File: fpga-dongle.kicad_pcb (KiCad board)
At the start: 2 copper layers, 85.8 x 137 mm, 119 parts, among them P1 USB_PWR, P2 PGM, P3 right, P4 left, P5 CONN_01X40, P6 CONN_01X40, P7 DBG_SWD, P8 USB_PWR, Q1 BC857, SW1 T1107A(6x3,8x2,5MM)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

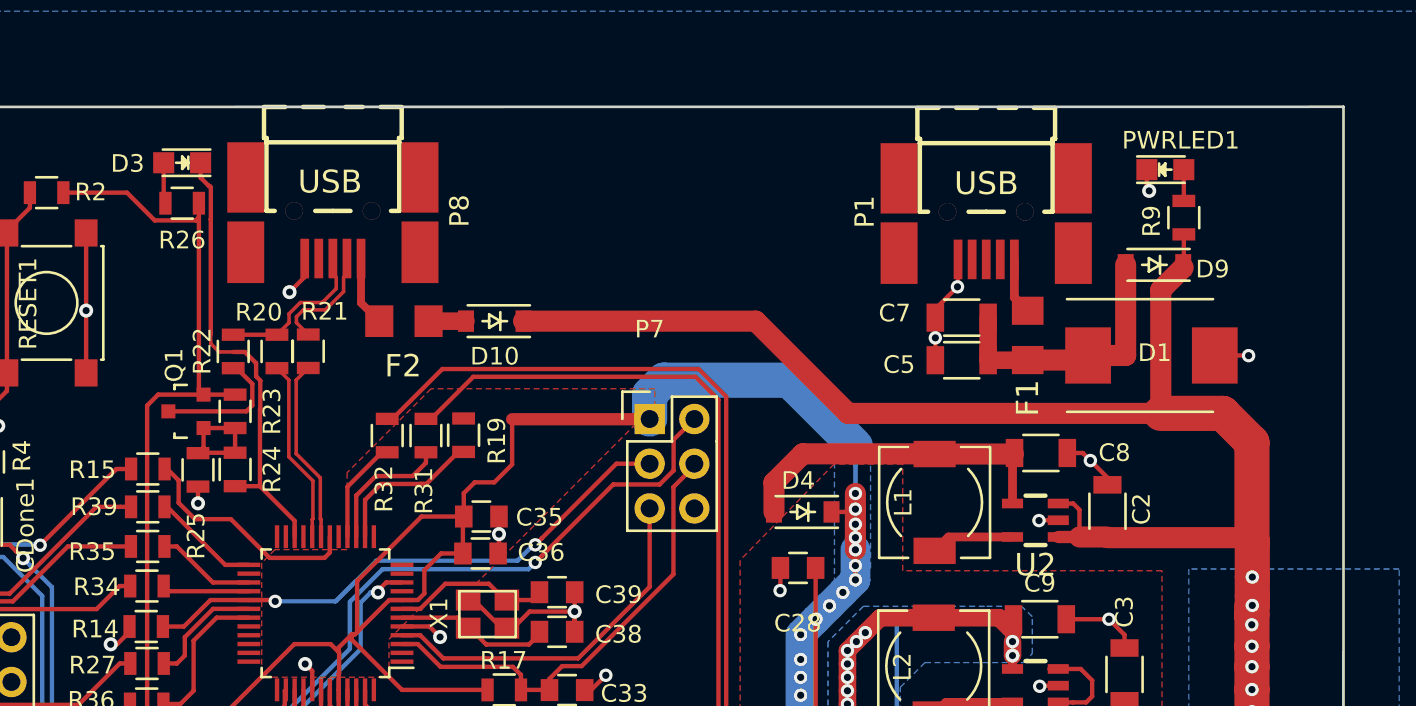
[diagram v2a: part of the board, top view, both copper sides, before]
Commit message: Change USB power-only connector by screw connector
Signed-off-by: Martin Ribelotta <martinribelotta@gmail.com>
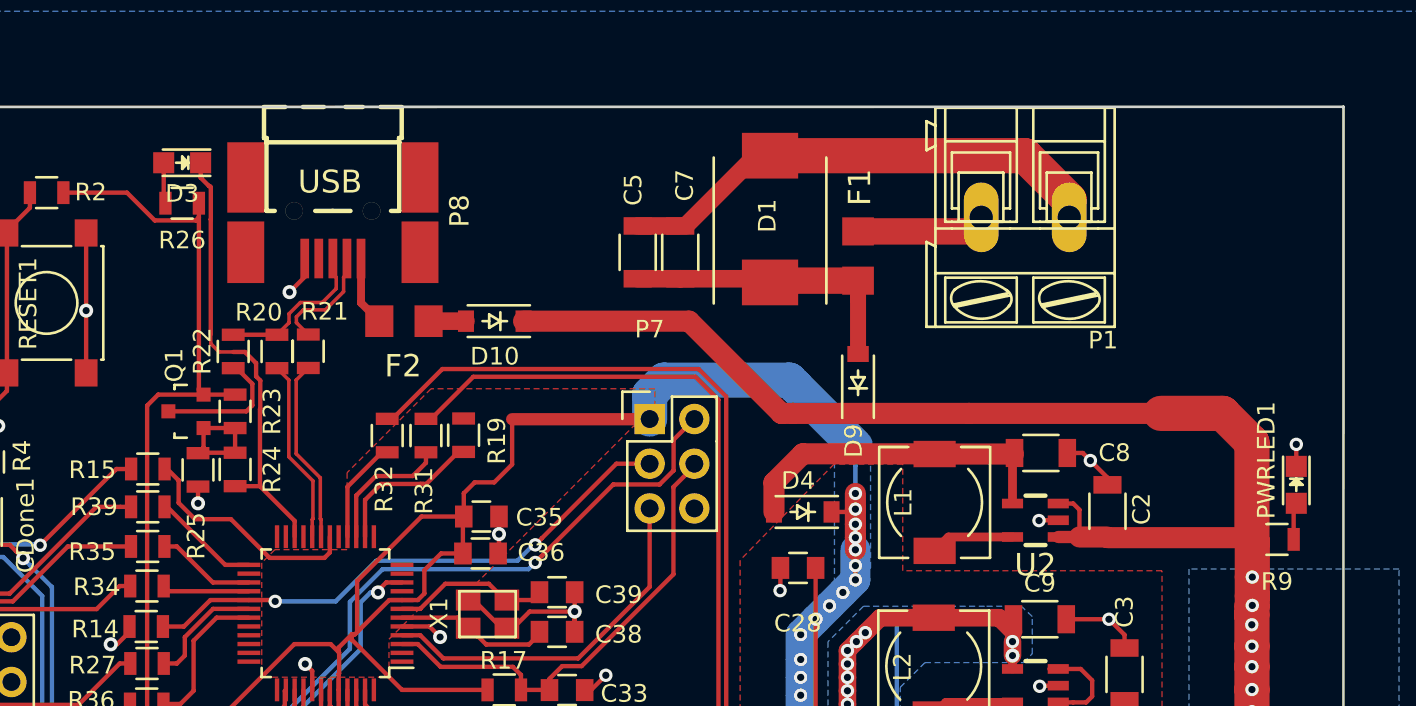
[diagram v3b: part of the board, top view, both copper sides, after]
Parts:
- D3: footprint LEDs:LED-0805 -> LEDs:LED_0805
- P1: value USB_PWR -> CONN_01X02; footprint OLIMEX_Connectors-FP:USB_Mini-B-NOSILK -> Connect:AK300-2
- moved D1 23.0 mm to (68.5, 24.0), turned to 90 degrees
- moved C5 19.4 mm to (61.0, 25.9), turned to 270 degrees
- moved PWRLED1 19.4 mm to (98.4, 39.1), turned to 270 degrees
- moved R9 19.0 mm to (97.3, 42.2), turned to 0 degrees
- moved D9 18.1 mm to (73.5, 33.3), turned to 90 degrees
- moved C7 16.4 mm to (63.4, 25.9), turned to 270 degrees
- moved F1 10.6 mm to (73.5, 26.1)
- moved P1 4.73 mm to (85.5, 23.9), turned to 180 degrees
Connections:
- P1 pad 1: Net-(F1-Pad1) -> GND
- P1 pad 2: (no net) -> Net-(F1-Pad1)
- P2 pad 7: (no net) -> Net-(P2-Pad7)
- P3 pad 10: (no net) -> Net-(P3-Pad10)
- P3 pad 22: (no net) -> /LCD4
- P3 pad 24: (no net) -> /LCD_RS
- P3 pad 26: (no net) -> /LCD3
- P3 pad 28: (no net) -> /LCD2
- P3 pad 30: (no net) -> /LCD1
- P3 pad 31: (no net) -> /GPIO2
- P3 pad 32: (no net) -> /GPIO1
- P3 pad 33: (no net) -> /GPIO4
- P3 pad 34: (no net) -> /GPIO3
- P3 pad 35: (no net) -> /GPIO6
- P3 pad 36: (no net) -> /GPIO5
- P3 pad 38: (no net) -> /GPIO7
- P3 pad 40: (no net) -> /GPIO8
- P3 pad 8: (no net) -> Net-(P3-Pad8)
- P3 pad 9: (no net) -> Net-(P3-Pad9)
- P4 pad 11: (no net) -> Net-(P4-Pad11)
- P4 pad 13: (no net) -> Net-(P4-Pad13)
- P4 pad 15: (no net) -> Net-(P4-Pad15)
- P4 pad 17: (no net) -> Net-(P4-Pad17)
- P4 pad 27: (no net) -> /CAN_RD
- P4 pad 29: (no net) -> /CAN_TD
- P4 pad 3: (no net) -> Net-(P4-Pad3)
- P4 pad 31: (no net) -> /T_COL1
- P4 pad 33: (no net) -> /T_FIL0
- P4 pad 34: (no net) -> /T_COL2
- P4 pad 35: (no net) -> /T_FIL3
- P4 pad 36: (no net) -> /T_FIL1
- P4 pad 37: (no net) -> /T_FIL2
- P4 pad 39: (no net) -> /T_COL0
- P4 pad 5: (no net) -> Net-(P4-Pad5)
- P4 pad 6: (no net) -> Net-(P4-Pad6)
- P4 pad 7: (no net) -> Net-(P4-Pad7)
- P4 pad 9: (no net) -> Net-(P4-Pad9)
- P5 pad 35: (no net) -> Net-(P5-Pad35)
- P5 pad 36: (no net) -> Net-(P5-Pad36)
- P5 pad 5: (no net) -> Net-(P5-Pad5)
- P5 pad 6: (no net) -> Net-(P5-Pad6)
- P5 pad 7: (no net) -> Net-(P5-Pad7)
- P5 pad 8: (no net) -> Net-(P5-Pad8)
- P6 pad 35: (no net) -> Net-(P6-Pad35)
- P6 pad 36: (no net) -> Net-(P6-Pad36)
- P6 pad 5: (no net) -> Net-(P6-Pad5)
- P6 pad 6: (no net) -> Net-(P6-Pad6)
- P8 pad 4: (no net) -> Net-(P8-Pad4)
- P8 pad 6: (no net) -> Net-(P8-Pad6)
- U4 pad 109: (no net) -> Net-(U4-Pad109)
- U4 pad 133: (no net) -> Net-(U4-Pad133)
- U4 pad 35: (no net) -> Net-(U4-Pad35)
- U4 pad 36: (no net) -> Net-(U4-Pad36)
- U4 pad 50: (no net) -> Net-(U4-Pad50)
- U4 pad 51: (no net) -> Net-(U4-Pad51)
- U4 pad 58: (no net) -> Net-(U4-Pad58)
- U4 pad 77: (no net) -> Net-(U4-Pad77)
- U5 pad 40: (no net) -> Net-(U5-Pad40)
- U6 pad 1: (no net) -> Net-(U6-Pad1)
- U6 pad 11: (no net) -> Net-(U6-Pad11)
- U6 pad 12: (no net) -> Net-(U6-Pad12)
- U6 pad 13: (no net) -> Net-(U6-Pad13)
- U6 pad 17: (no net) -> Net-(U6-Pad17)
- U6 pad 2: (no net) -> Net-(U6-Pad2)
- U6 pad 21: (no net) -> Net-(U6-Pad21)
- U6 pad 23: (no net) -> Net-(U6-Pad23)
- U6 pad 24: (no net) -> Net-(U6-Pad24)
- U6 pad 26: (no net) -> Net-(U6-Pad26)
- U6 pad 32: (no net) -> Net-(U6-Pad32)
- U6 pad 33: (no net) -> Net-(U6-Pad33)
- U6 pad 34: (no net) -> Net-(U6-Pad34)
- U6 pad 35: (no net) -> Net-(U6-Pad35)
- U6 pad 36: (no net) -> Net-(U6-Pad36)
- U6 pad 37: (no net) -> Net-(U6-Pad37)
- U6 pad 48: (no net) -> Net-(U6-Pad48)
- U6 pad 9: (no net) -> Net-(U6-Pad9)
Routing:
- net GND: track 278.4 -> 298.4 mm, vias 75 -> 72
- net Net-(F1-Pad1): track 3.23 -> 7.33 mm
- net +5V: track 262.9 -> 259.1 mm
- net Net-(C5-Pad2): track 15.5 -> 16.8 mm
